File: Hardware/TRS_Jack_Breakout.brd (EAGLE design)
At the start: 27.9 x 30.5 mm, 7 parts

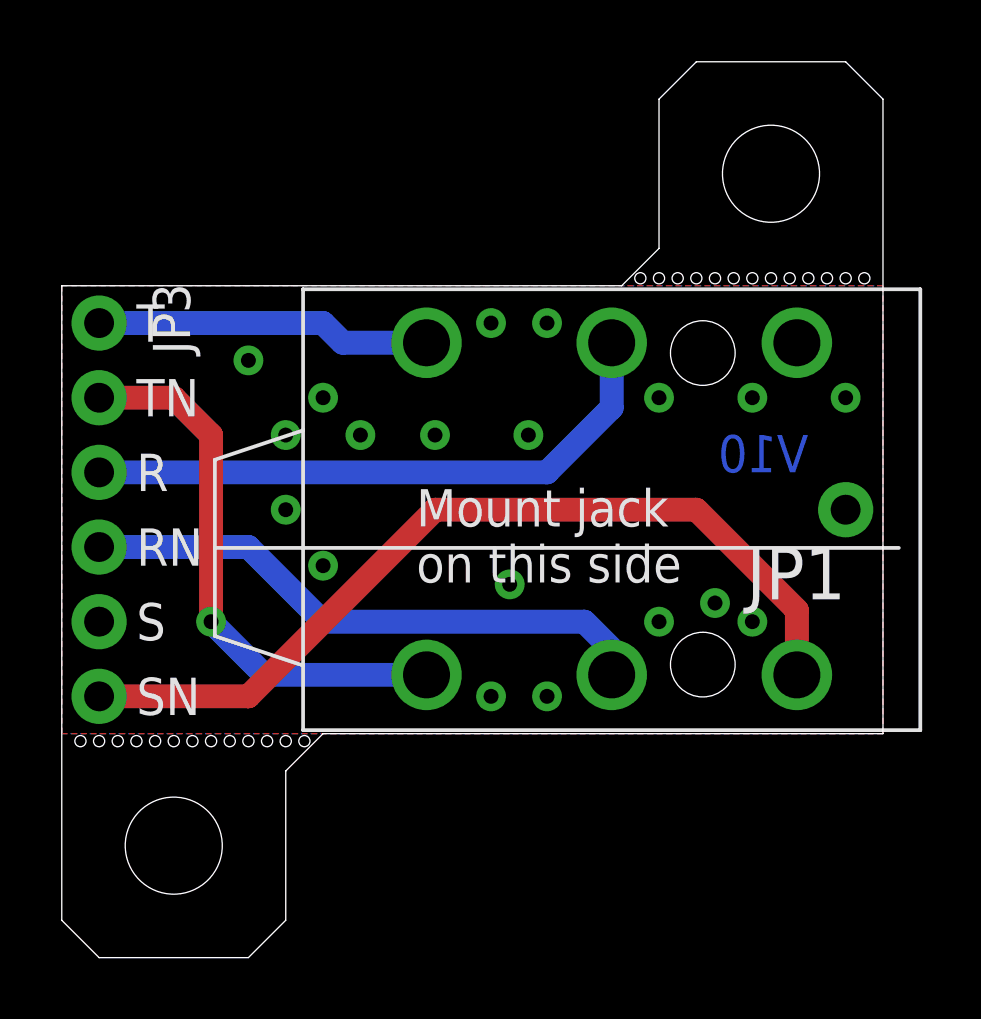
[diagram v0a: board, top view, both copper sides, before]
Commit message: Updates after red review.
Wider outline on dimension layer, added gear logo.
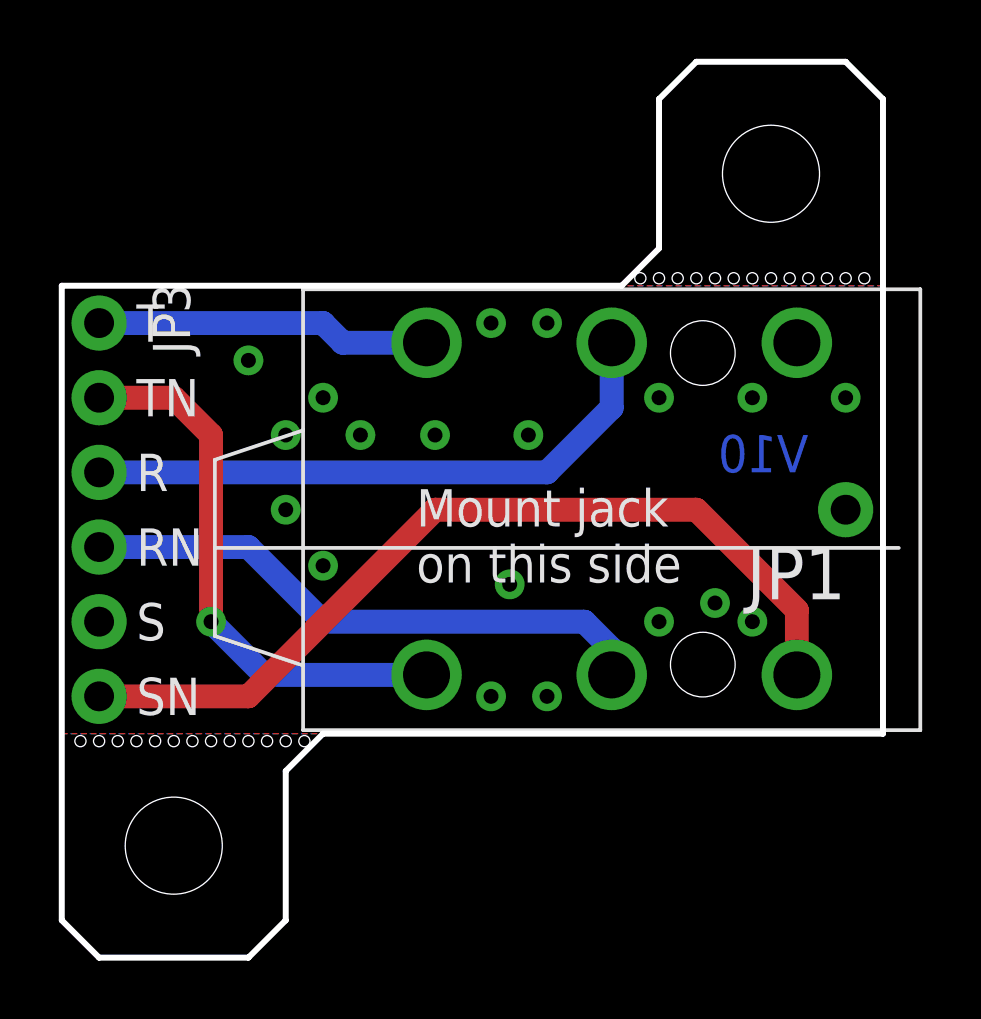
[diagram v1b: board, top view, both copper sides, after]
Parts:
- added LOGO2: OSHW-LOGOS, SparkFun-Aesthetics:OSHW-LOGO-S
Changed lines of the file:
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@@
 <layer number="17" name="Pads" color="2" fill="1" visible="yes" active="yes"/>
 <layer number="18" name="Vias" color="2" fill="1" visible="yes" active="yes"/>
-<layer number="19" name="Unrouted" color="6" fill="1" visible="yes" active="yes"/>
+<layer number="19" name="Unrouted" color="6" fill="1" visible="no" active="yes"/>
 <layer number="20" name="Dimension" color="15" fill="1" visible="yes" active="yes"/>
 <layer number="21" name="tPlace" color="16" fill="1" visible="yes" active="yes"/>
@@
 <layer number="43" name="vRestrict" color="2" fill="10" visible="no" active="yes"/>
 <layer number="44" name="Drills" color="7" fill="1" visible="no" active="yes"/>
-<layer number="45" name="Holes" color="7" fill="1" visible="yes" active="yes"/>
+<layer number="45" name="Holes" color="7" fill="1" visible="no" active="yes"/>
 <layer number="46" name="Milling" color="3" fill="1" visible="no" active="yes"/>
 <layer number="47" name="Measures" color="7" fill="1" visible="no" active="yes"/>
@@
 <layer number="49" name="Reference" color="7" fill="1" visible="no" active="yes"/>
 <layer number="50" name="dxf" color="7" fill="1" visible="no" active="no"/>
-<layer number="51" name="tDocu" color="6" fill="1" visible="yes" active="yes"/>
+<layer number="51" name="tDocu" color="6" fill="1" visible="no" active="yes"/>
 <layer number="52" name="bDocu" color="7" fill="1" visible="no" active="yes"/>
 <layer number="53" name="tGND_GNDA" color="7" fill="9" visible="no" active="no"/>
@@
 <board>
 <plain>
-<wire x1="27.94" y1="29.21" x2="26.67" y2="30.48" width="0" layer="20"/>
-<wire x1="26.67" y1="30.48" x2="21.59" y2="30.48" width="0" layer="20"/>
-<wire x1="21.59" y1="30.48" x2="20.32" y2="29.21" width="0" layer="20"/>
-<wire x1="20.32" y1="29.21" x2="20.32" y2="24.13" width="0" layer="20"/>
-<wire x1="20.32" y1="24.13" x2="19.05" y2="22.86" width="0" layer="20"/>
-<wire x1="19.05" y1="22.86" x2="0" y2="22.86" width="0" layer="20"/>
-<wire x1="0" y1="22.86" x2="0" y2="1.27" width="0" layer="20"/>
-<wire x1="0" y1="1.27" x2="1.27" y2="0" width="0" layer="20"/>
-<wire x1="1.27" y1="0" x2="6.35" y2="0" width="0" layer="20"/>
-<wire x1="6.35" y1="0" x2="7.62" y2="1.27" width="0" layer="20"/>
-<wire x1="7.62" y1="1.27" x2="7.62" y2="6.35" width="0" layer="20"/>
-<wire x1="7.62" y1="6.35" x2="8.89" y2="7.62" width="0" layer="20"/>
-<wire x1="8.89" y1="7.62" x2="27.94" y2="7.62" width="0" layer="20"/>
-<wire x1="27.94" y1="7.62" x2="27.94" y2="29.21" width="0" layer="20"/>
+<wire x1="27.94" y1="29.21" x2="26.67" y2="30.48" width="0.2032" layer="20"/>
+<wire x1="26.67" y1="30.48" x2="21.59" y2="30.48" width="0.2032" layer="20"/>
+<wire x1="21.59" y1="30.48" x2="20.32" y2="29.21" width="0.2032" layer="20"/>
+<wire x1="20.32" y1="29.21" x2="20.32" y2="24.13" width="0.2032" layer="20"/>
+<wire x1="20.32" y1="24.13" x2="19.05" y2="22.86" width="0.2032" layer="20"/>
+<wire x1="19.05" y1="22.86" x2="0" y2="22.86" width="0.2032" layer="20"/>
+<wire x1="0" y1="22.86" x2="0" y2="1.27" width="0.2032" layer="20"/>
+<wire x1="0" y1="1.27" x2="1.27" y2="0" width="0.2032" layer="20"/>
+<wire x1="1.27" y1="0" x2="6.35" y2="0" width="0.2032" layer="20"/>
+<wire x1="6.35" y1="0" x2="7.62" y2="1.27" width="0.2032" layer="20"/>
+<wire x1="7.62" y1="1.27" x2="7.62" y2="6.35" width="0.2032" layer="20"/>
+<wire x1="7.62" y1="6.35" x2="8.89" y2="7.62" width="0.2032" layer="20"/>
+<wire x1="8.89" y1="7.62" x2="27.94" y2="7.62" width="0.2032" layer="20"/>
+<wire x1="27.94" y1="7.62" x2="27.94" y2="29.21" width="0.2032" layer="20"/>
 <text x="2.54" y="21.59" size="1.27" layer="21" font="vector" ratio="15" align="center-left">T</text>
 <text x="2.54" y="19.05" size="1.27" layer="21" font="vector" ratio="15" align="center-left">TN</text>
@@
 <element name="STANDOFF2" library="SparkFun-Electromechanical" package="STAND-OFF" value="STAND-OFF" x="3.81" y="3.81"/>
 <element name="JP2" library="SparkFun-Connectors" package="1X01NS" value="M01SMDNS" x="26.67" y="15.24"/>
+<element name="LOGO2" library="SparkFun-Aesthetics" package="OSHW-LOGO-S" value="OSHW-LOGOS" x="10.16" y="15.24" rot="MR0"/>
 </elements>
 <signals>
